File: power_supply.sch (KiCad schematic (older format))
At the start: 69 parts, among them J1 12v, 0.5A nominal, 5A Surge, J2 Power Switch, J3 Shutdown, J4 12V 5V, J5 Program, J6 Serial Debug, J7 REMOVE to PRGM, J8 5V 25W, J9 FRAM I2C, M1 XL4015, M2 U1V11F5, M3 U3V70F5, Q1 BSS806, Q2 BSS806, Q3 SPD18P06PGBTMA1, Q4 BSS806, Q5 BSS806, Q6 SQ3495-EV, U1 MCP9700A, U2 BTS443P, U3 ALD910027, U4 PIC16F1709, U5 MCP111-195, U6 MB85RC1MT, U7 MCP1700-3302E_SOT23

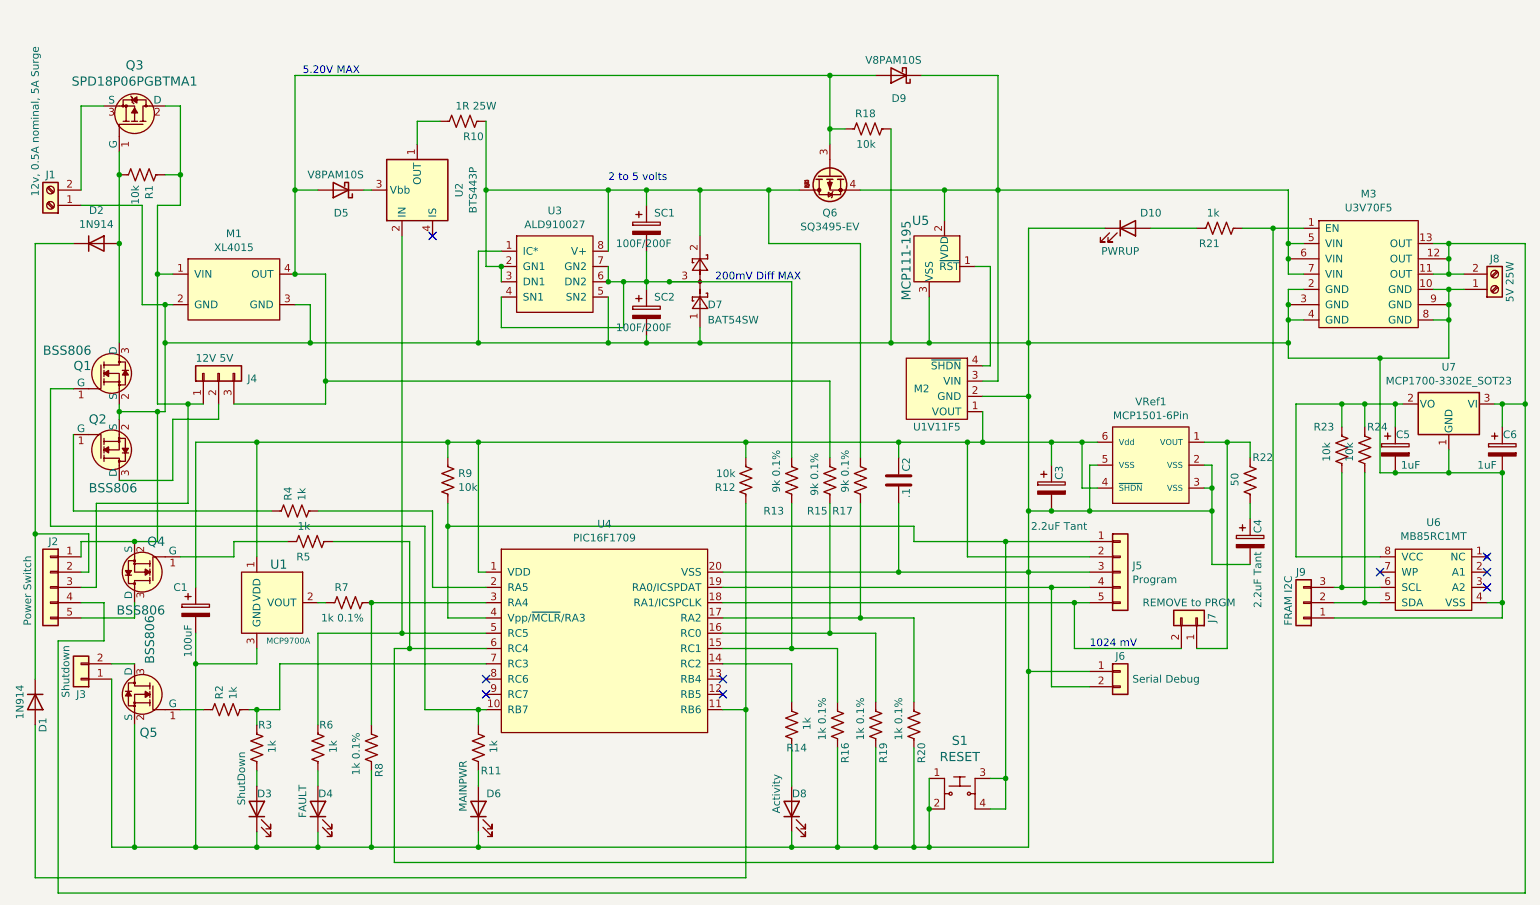
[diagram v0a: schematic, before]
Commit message: Version 1.01 - Includes fixes, footprint validation, gerbers, screenshots, documentation
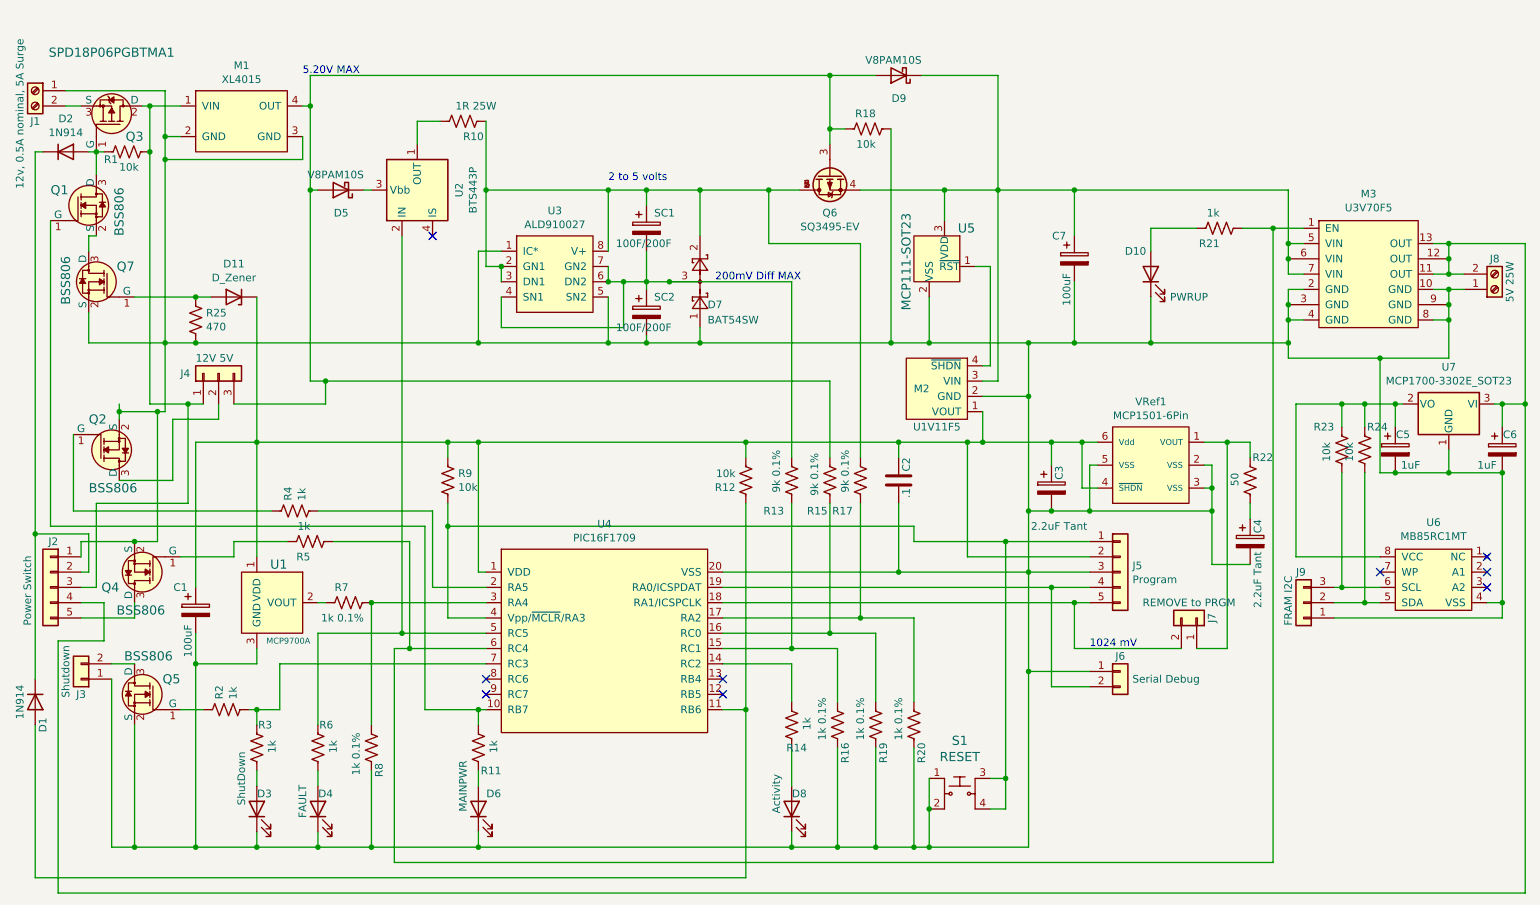
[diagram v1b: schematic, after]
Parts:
- removed U5: MCP111-195, digikey-footprints:SOT-23-3, symbol dk_PMIC-Supervisors:MCP130T-300I_TT
- added C7: 100uF, Capacitor_SMD:CP_Elec_6.3x5.2, symbol Device:CP
- added D11: D_Zener, Diode_SMD:D_SOD-123F, symbol Device:D_Zener
- added Q7: BSS806, digikey-footprints:SOT-23-3, symbol dk_Transistors-FETs-MOSFETs-Single:BSS138
- added R25: 470, Resistor_SMD:R_1206_3216Metric, symbol Device:R_US
- added U5: MCP111-SOT23, digikey-footprints:SOT-23-3, symbol Geekgineering:MCP111-SOT23
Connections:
- net at C1.2, C2.1, C3.2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: now also C7.2, Q7.2 (S), R25.1, U5.2 (VSS); no longer Q1.2 (S)
- net at D9.1 (K), M2.3 (VIN), M3.5 (VIN)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: now also C7.1, U5.3 (VDD)
- net at C1.1, C2.2, C3.1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: now also D11.1 (K)
- net at M2.4 (~SHDN): now also U5.1 (~RST)
- new net: Q1.2 (S), Q7.3 (D)
- new net: D11.2 (A), Q7.1 (G), R25.2
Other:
- moved on the sheet: D10, D2, J1, M1, Q1, Q3, R1
